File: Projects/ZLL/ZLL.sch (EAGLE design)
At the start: 18 parts, among them IC1 BMD-340-A-R, U1 BSS138BKW, X1 USB-MICROB, Y3 32.768kHz

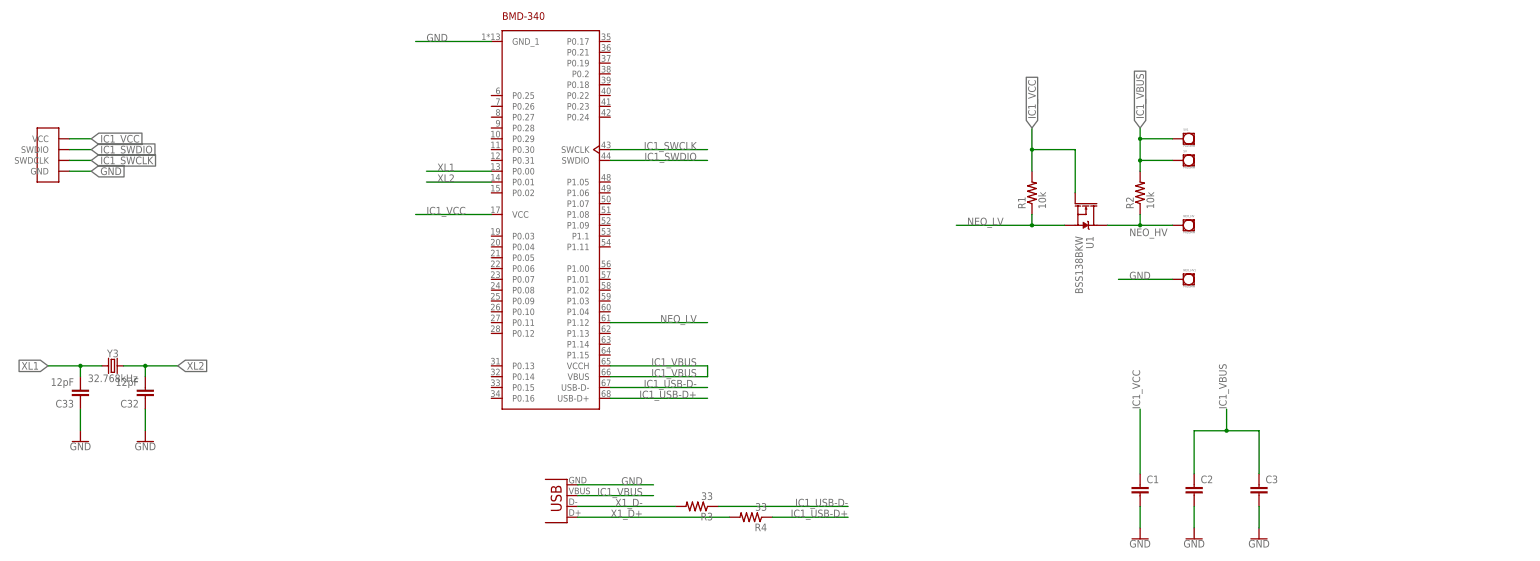
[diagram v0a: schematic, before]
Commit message: Added buttons on ZLL Added pads on nRF51 key SD prog finished N5 lib updated
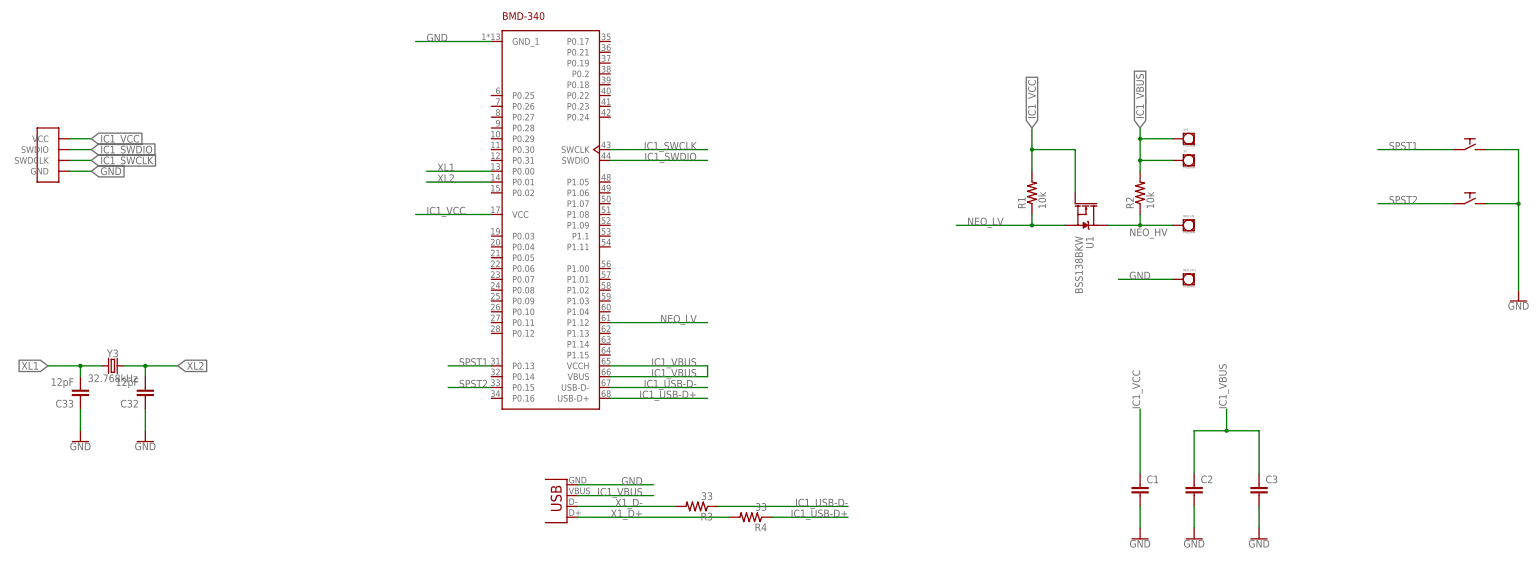
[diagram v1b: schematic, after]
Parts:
- added SPST1, SPST2: PTS526SK08, SPST:PTS526SK08
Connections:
- new net SPST1: IC1.P0.13, SPST1.P$1
- new net SPST2: IC1.P0.15, SPST2.P$1
- net GND: now also SPST1.P$2, SPST2.P$2
